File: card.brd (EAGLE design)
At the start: 84.8 x 53.3 mm, 56 parts, among them IC1 ATTINY1616, IC2 LTC1992, IC3 LTC1992, IC4 LTC6911, IC5 LTC2402, SW1 SPST_TACT-EVQQ2, SW2 SPST_TACT-EVQQ2, SW3 SPST_TACT-EVQQ2, SW4 SPST_TACT-EVQQ2

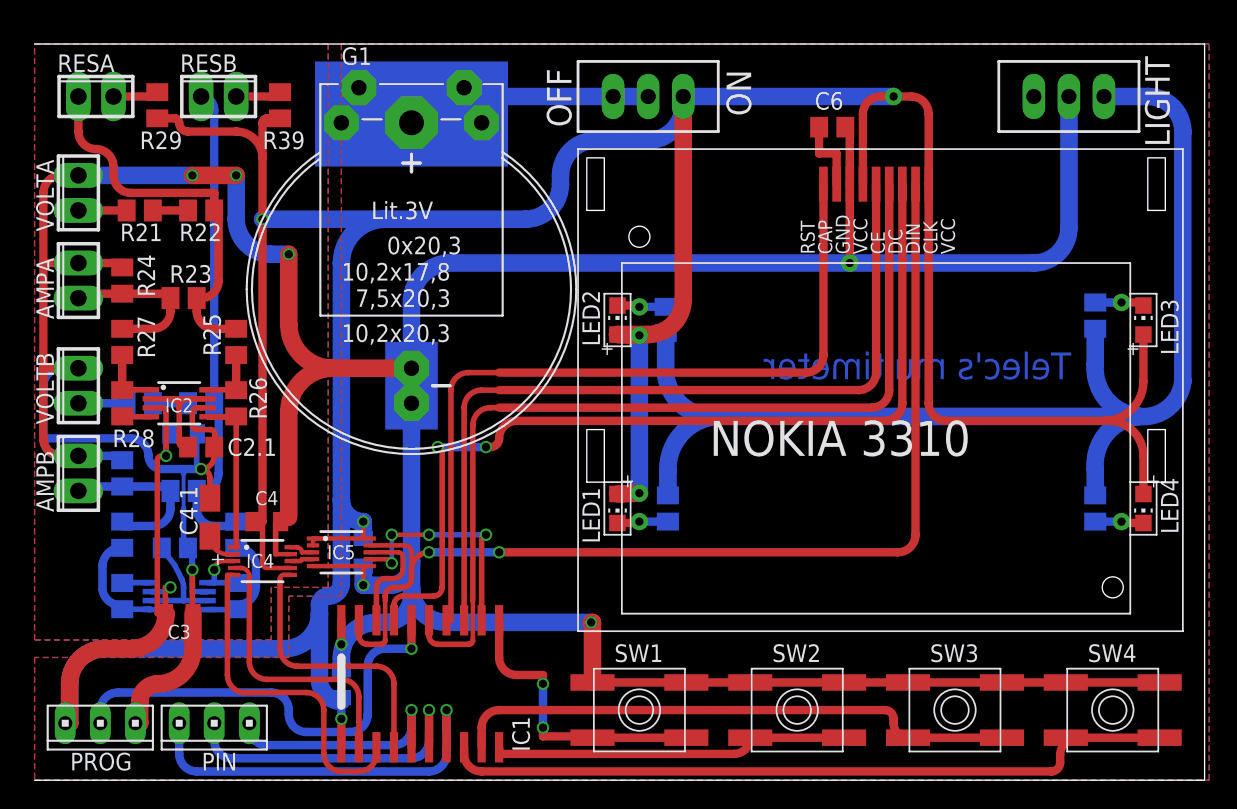
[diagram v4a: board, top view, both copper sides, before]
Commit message: Added missing dimension
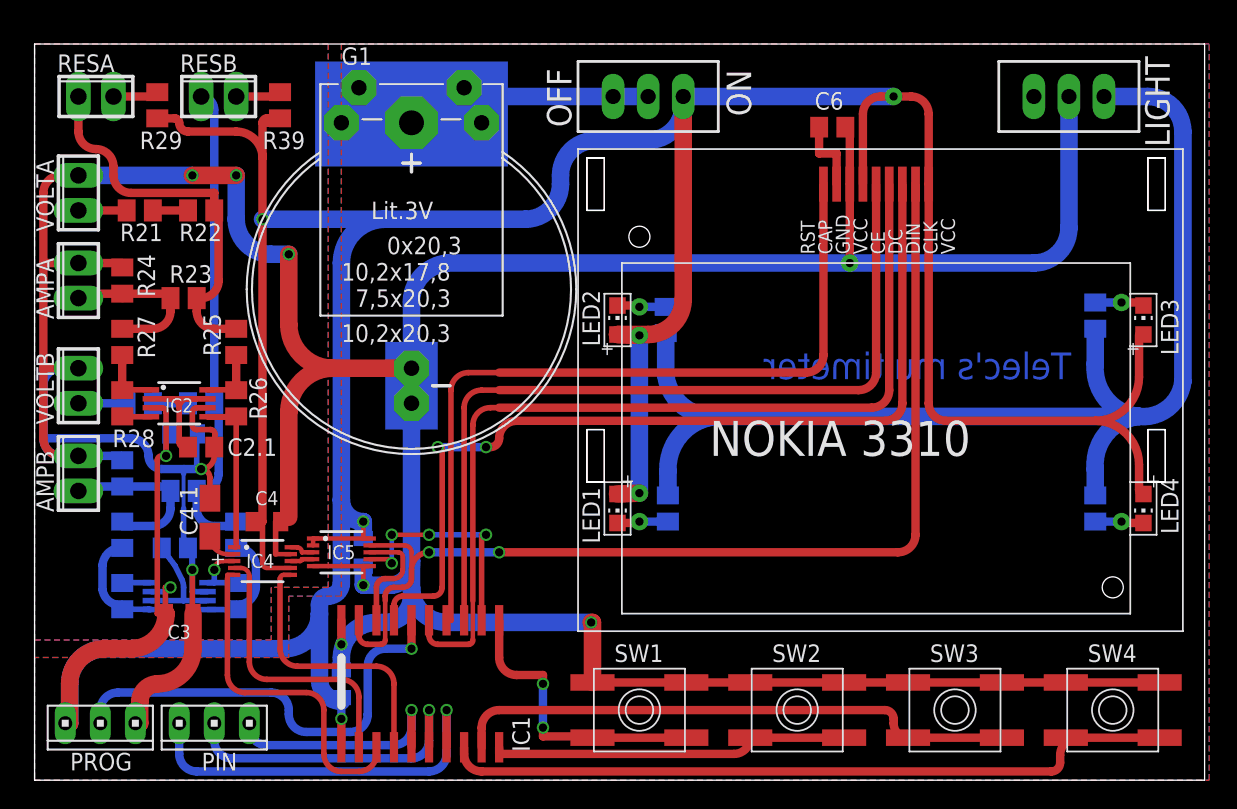
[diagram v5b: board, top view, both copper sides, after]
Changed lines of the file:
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@@
 <?xml version="1.0" encoding="utf-8"?>
 <!DOCTYPE eagle SYSTEM "eagle.dtd">
-<eagle version="7.6.0">
+<eagle version="7.7.0">
 <drawing>
 <settings>
@@
 <setting verticaltext="up"/>
 </settings>
-<grid distance="0.75" unitdist="mil" unit="mil" style="lines" multiple="1" display="yes" altdistance="0.00625" altunitdist="inch" altunit="inch"/>
+<grid distance="0.025" unitdist="inch" unit="inch" style="lines" multiple="1" display="yes" altdistance="0.00625" altunitdist="inch" altunit="inch"/>
 <layers>
 <layer number="1" name="Top" color="4" fill="1" visible="yes" active="yes"/>
@@
 <layer number="27" name="tValues" color="7" fill="1" visible="yes" active="yes"/>
 <layer number="28" name="bValues" color="7" fill="1" visible="yes" active="yes"/>
-<layer number="29" name="tStop" color="7" fill="3" visible="yes" active="yes"/>
-<layer number="30" name="bStop" color="7" fill="6" visible="yes" active="yes"/>
+<layer number="29" name="tStop" color="7" fill="3" visible="no" active="yes"/>
+<layer number="30" name="bStop" color="7" fill="6" visible="no" active="yes"/>
 <layer number="31" name="tCream" color="7" fill="4" visible="yes" active="yes"/>
 <layer number="32" name="bCream" color="7" fill="5" visible="yes" active="yes"/>
@@
 <rectangle x1="46.682025" y1="10.048875" x2="75.333225" y2="10.067925" layer="26" rot="R180"/>
 <text x="75.38085" y="0.9144" size="0.0381" layer="26" font="vector" rot="MR0">F:/Users/Loup/Doc/eagle/Logo/logoBW.bmp</text>
+<wire x1="0" y1="0" x2="0" y2="53.32095" width="0" layer="20"/>
 </plain>
 <attributes>
@@
 <contactref element="LED4" pad="A"/>
 <contactref element="LED3" pad="A"/>
-<wire x1="77.7875" y1="26.035" x2="77.47" y2="26.035" width="0.6096" layer="1"/>
-<wire x1="77.47" y1="26.035" x2="66.04" y2="26.035" width="0.6096" layer="1"/>
+<wire x1="76.835" y1="26.035" x2="66.04" y2="26.035" width="0.6096" layer="1"/>
 <wire x1="66.04" y1="26.035" x2="64.77" y2="27.305" width="0.6096" layer="1" curve="-90"/>
 <wire x1="64.77" y1="27.305" x2="64.77" y2="43.18" width="0.6096" layer="1"/>
@@
 <wire x1="44.45" y1="46.355" x2="46.99" y2="48.895" width="1.27" layer="16" curve="90"/>
 <wire x1="46.99" y1="48.895" x2="46.99" y2="49.53" width="1.27" layer="16"/>
-<wire x1="46.99" y1="46.355" x2="46.99" y2="43.18" width="0" layer="19" extent="1-16"/>
 <wire x1="25.4" y1="40.64" x2="35.56" y2="40.64" width="1.27" layer="16"/>
 <wire x1="35.56" y1="40.64" x2="38.1" y2="43.18" width="1.27" layer="16" curve="90"/>
@@
 <wire x1="11.1125" y1="46.99" x2="14.605" y2="46.99" width="0.6096" layer="1"/>
 <wire x1="14.605" y1="46.99" x2="16.51" y2="45.085" width="0.6096" layer="1" curve="-90"/>
-<wire x1="80.3275" y1="20.735" x2="80.3275" y2="23.495" width="0.6096" layer="1"/>
-<wire x1="80.3275" y1="23.495" x2="77.7875" y2="26.035" width="0.6096" layer="1" curve="90"/>
-<wire x1="80.3275" y1="32.2875" x2="80.3275" y2="28.8925" width="0.6096" layer="1"/>
-<wire x1="80.3275" y1="28.8925" x2="77.47" y2="26.035" width="0.6096" layer="1" curve="-90"/>
 <wire x1="16.8275" y1="15.375" x2="16.51" y2="15.6925" width="0.3302" layer="1" curve="-90"/>
 <wire x1="16.51" y1="15.6925" x2="16.51" y2="15.875" width="0.3302" layer="1"/>
 <wire x1="16.51" y1="15.875" x2="16.51" y2="18.7325" width="0.4064" layer="1"/>
+<wire x1="76.835" y1="26.035" x2="80.01" y2="22.86" width="0.6096" layer="1" curve="-90"/>
+<wire x1="80.01" y1="22.86" x2="80.01" y2="21.0525" width="0.6096" layer="1"/>
+<wire x1="80.01" y1="21.0525" x2="80.3275" y2="20.735" width="0.6096" layer="1" curve="90"/>
+<wire x1="76.835" y1="26.035" x2="80.01" y2="29.21" width="0.6096" layer="1" curve="90"/>
+<wire x1="80.01" y1="29.21" x2="80.01" y2="32.22625" width="0.6096" layer="1"/>
+<wire x1="80.01" y1="32.22625" x2="80.3275" y2="32.54375" width="0.6096" layer="1" curve="90"/>
+<wire x1="80.3275" y1="32.54375" x2="80.3275" y2="32.2875" width="0.6096" layer="1"/>
 </signal>
 <signal name="N$2">
